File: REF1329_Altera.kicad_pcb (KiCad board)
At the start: 2 copper layers, 102 x 71 mm, 42 parts, among them J1 DB25_Male, J3 Edge_Connector, J4 Edge_Connector, J6 Conn_02x05_Odd_Even, SW1 SW_Push, U1 SST28LF040, U2 SST28LF040, U3 HDSP-7501, U4 74HC164, U5 74HC04, U6 74HC374, U7 EPM240T100, X1 ASCO

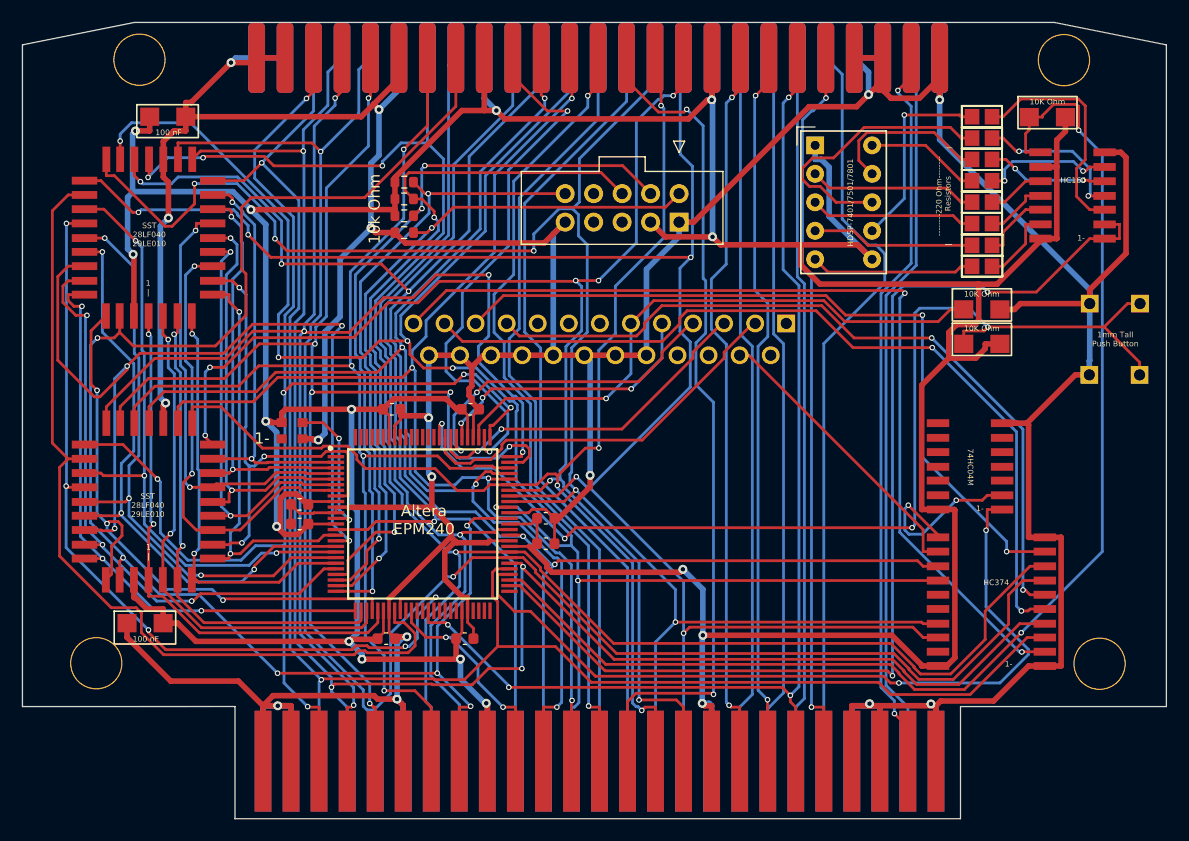
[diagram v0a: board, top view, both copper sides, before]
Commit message: Add RWeick, LibreShark, and timestamp to PCB silkscreen
Also make existing silkscreen text larger and avoid overlapping with holes in the board
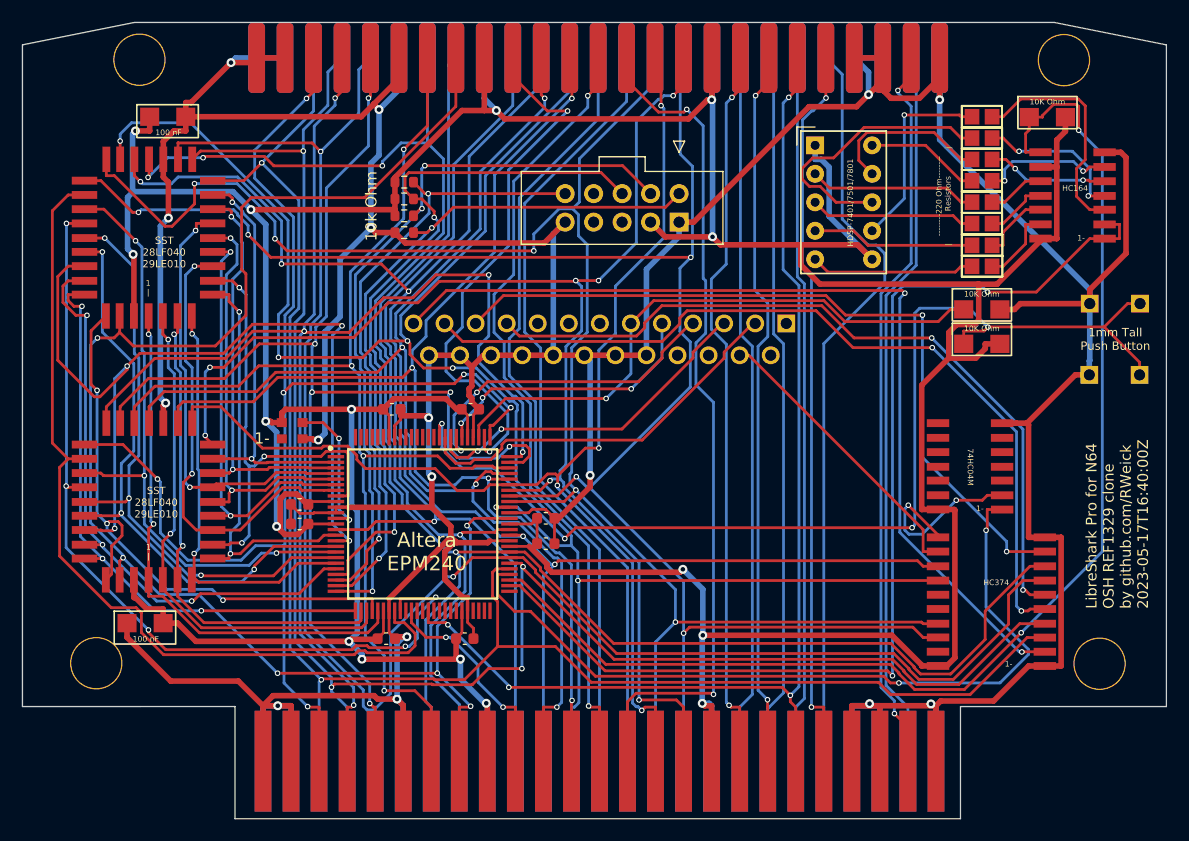
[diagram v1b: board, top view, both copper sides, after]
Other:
- board text added: "LibreShark Pro for N64 OSH REF1329 clone by github.com/RWeick 2023-05-17T16:40:00Z"
